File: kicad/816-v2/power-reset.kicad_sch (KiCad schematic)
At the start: 11 parts, among them J1 Barrel_Jack, SW1 SW_SPST, SW2 SW_Push, U12 DS1813-5

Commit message: Update KiCad files new pcb revision, hopefully working
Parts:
- VR1: value UA78L05ACPK -> 7805
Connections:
- net RESB renamed ~{RES}
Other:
- note added: "Alternative: TSR-1-2450 switch-mode regulator"
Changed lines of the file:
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@@
 		(title "Power and reset")
+	)
+	(text "Alternative: TSR-1-2450 switch-mode regulator"
+		(exclude_from_sim yes)
+		(at 138.43 71.12 0)
+		(effects
+			(font
+				(size 1.27 1.27)
+			)
+		)
 	)
 	(junction
@@
 		)
 	)
-	(global_label "RESB"
+	(global_label "~{RES}"
 		(shape output)
 		(at 209.55 90.17 0)
@@
 		)
 		(property "Intersheetrefs" "${INTERSHEET_REFS}"
-			(at 217.4337 90.17 0)
+			(at 216.1637 90.17 0)
 			(effects
 				(font
@@
 					(size 1.27 1.27)
 				)
+				(hide yes)
 			)
 		)
@@
 					(size 1.27 1.27)
 				)
+				(hide yes)
 			)
 		)
@@
 					(size 1.27 1.27)
 				)
+				(hide yes)
 			)
 		)
@@
 					(size 1.27 1.27)
 				)
+				(hide yes)
 			)
 		)
@@
 					(size 1.27 1.27)
 				)
+				(hide yes)
 			)
 		)
@@
 					(size 1.27 1.27)
 				)
+				(hide yes)
 			)
 		)
@@
 					(size 1.27 1.27)
 				)
+				(hide yes)
 			)
 		)
@@
 					(size 1.27 1.27)
 				)
+				(hide yes)
 			)
 		)
@@
 					(size 1.27 1.27)
 				)
+				(hide yes)
 			)
 		)
@@
 			)
 		)
-		(property "Value" "UA78L05ACPK"
+		(property "Value" "7805"
 			(at 137.16 54.61 0)
 			(effects

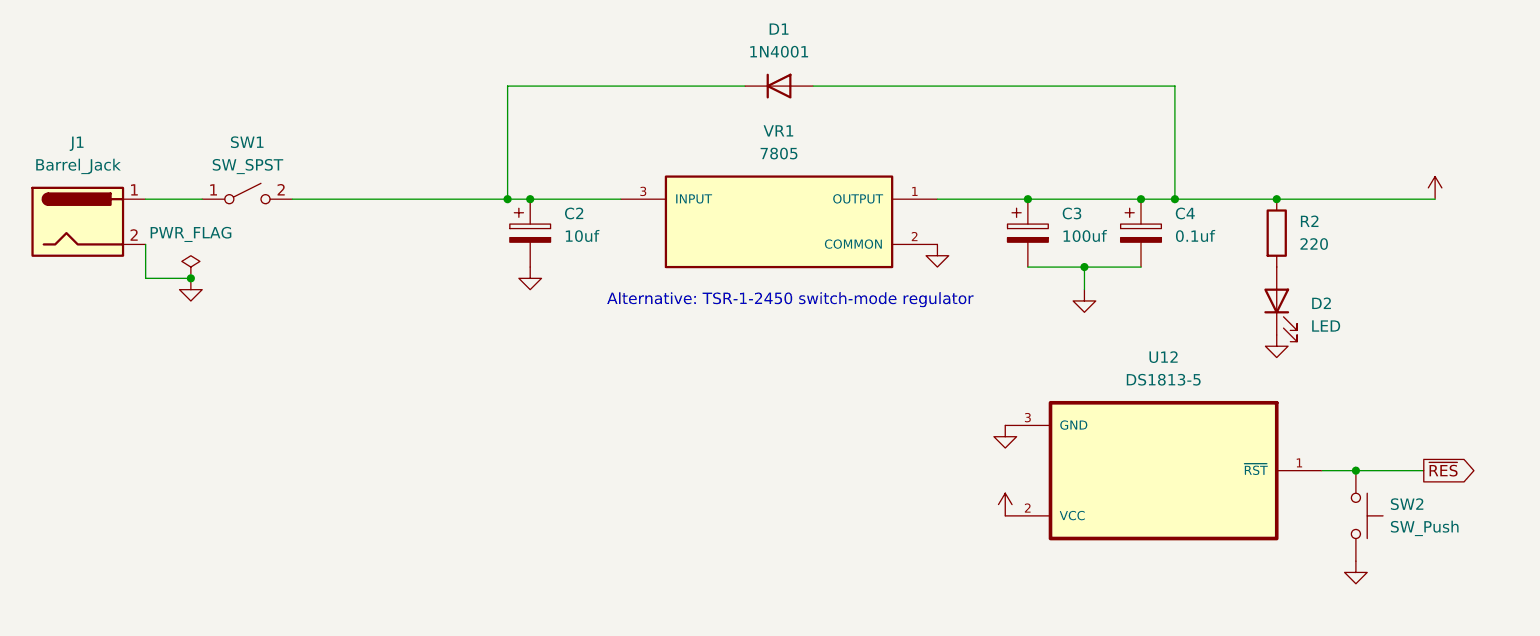
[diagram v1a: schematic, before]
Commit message: Update KiCad files to reflect ROM WE bodge
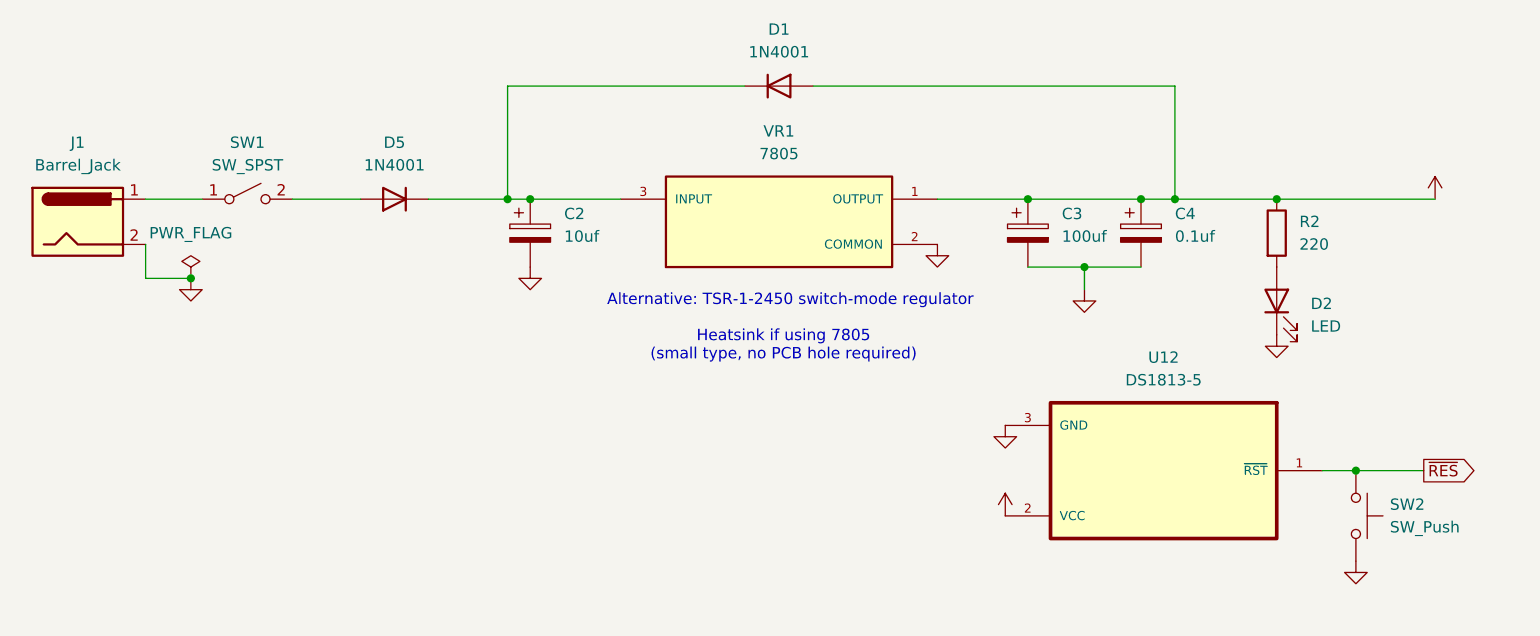
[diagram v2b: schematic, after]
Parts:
- added D5: 1N4001, Diode_THT:D_DO-41_SOD81_P10.16mm_Horizontal, symbol Diode:1N4001
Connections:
- net at C2.1, D1.1 (K), VR1.3 (INPUT): now also D5.1 (K); no longer SW1.2 (B)
- new net: D5.2 (A), SW1.2 (B)
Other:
- note added: "Heatsink if using 7805 (small type, no PCB hole required)"
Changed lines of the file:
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@@
 		(title "Power and reset")
+	)
+	(text "Heatsink if using 7805\n(small type, no PCB hole required)"
+		(exclude_from_sim no)
+		(at 137.668 76.2 0)
+		(effects
+			(font
+				(size 1.27 1.27)
+			)
+		)
 	)
 	(text "Alternative: TSR-1-2450 switch-mode regulator"
@@
 	)
 	(junction
-		(at 106.68 59.69)
-		(diameter 0)
-		(color 0 0 0 0)
-	)
-	(junction
 		(at 177.8 59.69)
 		(diameter 0)
@@
 	)
 	(junction
+		(at 106.68 59.69)
+		(diameter 0)
+		(color 0 0 0 0)
+	)
+	(junction
 		(at 193.04 59.69)
 		(diameter 0)
@@
 	(wire
 		(pts
+			(xy 97.79 59.69) (xy 106.68 59.69)
+		)
+		(stroke
+			(width 0)
+			(type default)
+		)
+	)
+	(wire
+		(pts
 			(xy 109.22 59.69) (xy 106.68 59.69)
 		)
@@
 	(wire
 		(pts
+			(xy 82.55 59.69) (xy 90.17 59.69)
+		)
+		(stroke
+			(width 0)
+			(type default)
+		)
+	)
+	(wire
+		(pts
 			(xy 66.04 59.69) (xy 72.39 59.69)
 		)
@@
 		(pts
 			(xy 177.8 59.69) (xy 181.61 59.69)
-		)
-		(stroke
-			(width 0)
-			(type default)
-		)
-	)
-	(wire
-		(pts
-			(xy 82.55 59.69) (xy 106.68 59.69)
 		)
 		(stroke
@@
 					(unit 1)
 				)
+			)
+		)
+	)
+	(symbol
+		(lib_id "Diode:1N4001")
+		(at 93.98 59.69 180)
+		(unit 1)
+		(exclude_from_sim no)
+		(in_bom yes)
+		(on_board yes)
+		(dnp no)
+		(fields_autoplaced yes)
+		(property "Reference" "D5"
+			(at 93.98 53.34 0)
+			(effects
+				(font
+					(size 1.27 1.27)
+				)
+			)
+		)
+		(property "Value" "1N4001"
+			(at 93.98 55.88 0)
+			(effects
+				(font
+					(size 1.27 1.27)
+				)
+			)
+		)
+		(property "Footprint" "Diode_THT:D_DO-41_SOD81_P10.16mm_Horizontal"
+			(at 93.98 59.69 0)
+			(effects
+				(font
+					(size 1.27 1.27)
+				)
+				(hide yes)
+			)
+		)
+		(property "Datasheet" "http://www.vishay.com/docs/88503/1n4001.pdf"
+			(at 93.98 59.69 0)
+			(effects
+				(font
+					(size 1.27 1.27)
+				)
+				(hide yes)
+			)
+		)
+		(property "Description" "50V 1A General Purpose Rectifier Diode, DO-41"
+			(at 93.98 59.69 0)
+			(effects
+				(font
+					(size 1.27 1.27)
+				)
+				(hide yes)
+			)
+		)
+		(property "Sim.Device" "D"
+			(at 93.98 59.69 0)
+			(effects
+				(font
+					(size 1.27 1.27)
+				)
+				(hide yes)
+			)
+		)
+		(property "Sim.Pins" "1=K 2=A"
+			(at 93.98 59.69 0)
+			(effects
+				(font
+					(size 1.27 1.27)
+				)
+				(hide yes)
+			)
+		)
+		(pin "2"
+		)
+		(pin "1"
+		)
+		(instances
+			(project ""
+				(path "/58394049-29b8-4f07-ad62-86008e573e13/c500074a-9789-4561-8bac-70bcad3a7917"
+					(reference "D5")
+					(unit 1)
+				)
